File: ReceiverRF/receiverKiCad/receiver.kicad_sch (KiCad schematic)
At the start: 23 parts, among them U1 STM32F103RET6, Y1 Crystal_GND24

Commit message: choix ferrite bead et footprint
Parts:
- FB?: footprint (none) -> Footprints:Ferrite_0603
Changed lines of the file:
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@@
 			)
 		)
-		(property "Footprint" ""
+		(property "Footprint" "Footprints:Ferrite_0603"
 			(at 187.96 35.052 90)
 			(effects
@@
 			)
 		)
-		(property "Datasheet" "Ferrite bead"
+		(property "Datasheet" "https://www.digikey.ca/en/products/detail/vishay-dale/ILBB0603ER121V/2574888"
 			(at 187.96 36.83 0)
 			(effects
@@
 			)
 		)
-		(property "Description" ""
+		(property "Description" "120 ohm @ 100 MHz"
 			(at 187.96 36.83 0)
 			(effects

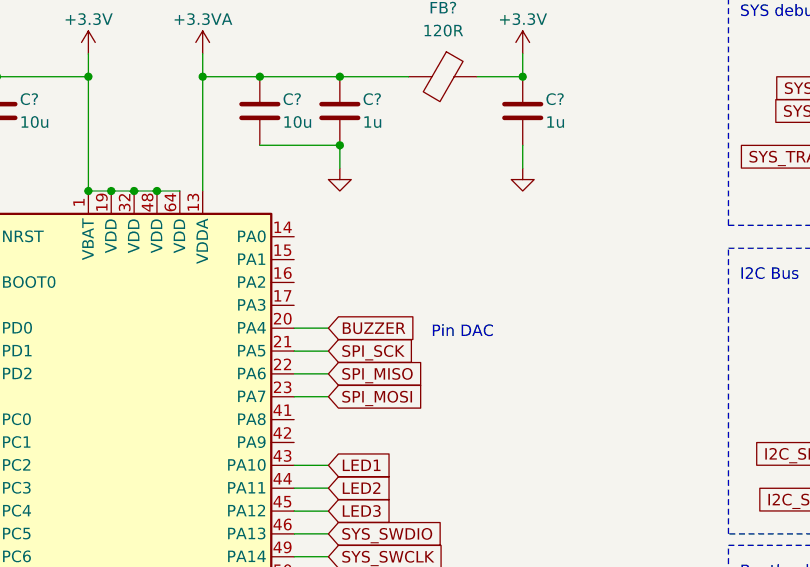
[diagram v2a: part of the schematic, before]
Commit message: Corrige path footprints
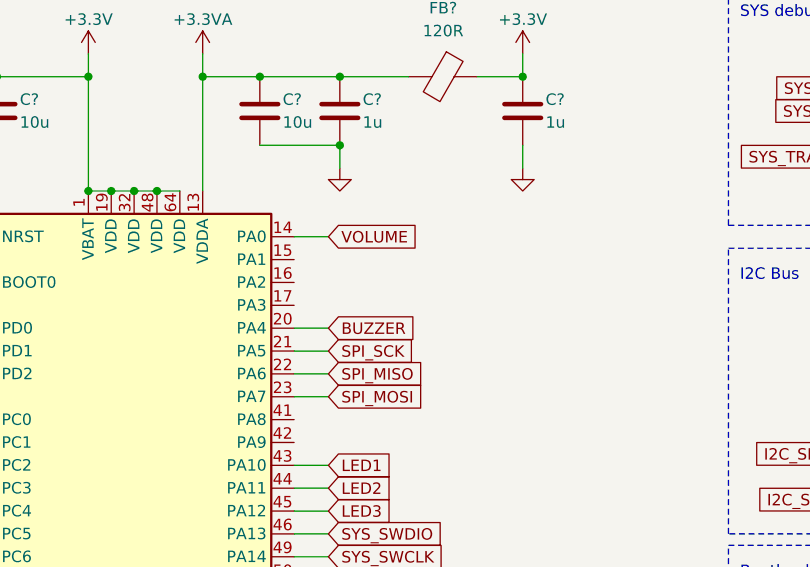
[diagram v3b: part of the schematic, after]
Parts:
- U1: footprint footprint-receiver:LQFP64-10x10mm -> Footprints:LQFP64-10x10mm
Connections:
- net VOLUME: now reaches U1.14 (PA0)
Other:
- note removed: "Pin DAC"
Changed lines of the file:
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@@
+	(wire
+		(pts
+			(xy 171.45 54.61) (xy 175.26 54.61)
+		)
+		(stroke
+			(width 0)
+			(type default)
+		)
+	)
 	(wire
 		(pts
@@
 		)
 	)
-	(text "Pin DAC"
-		(exclude_from_sim no)
-		(at 186.69 66.04 0)
-		(effects
-			(font
-				(size 1.27 1.27)
-			)
-			(justify left bottom)
-		)
-	)
 	(text "SYS debug\n"
 		(exclude_from_sim no)
@@
 		(property "Intersheetrefs" "${INTERSHEET_REFS}"
 			(at 186.8328 135.89 0)
+			(effects
+				(font
+					(size 1.27 1.27)
+				)
+				(justify left)
+				(hide yes)
+			)
+		)
+	)
+	(global_label "VOLUME"
+		(shape input)
+		(at 175.26 54.61 0)
+		(fields_autoplaced yes)
+		(effects
+			(font
+				(size 1.27 1.27)
+			)
+			(justify left)
+		)
+		(property "Intersheetrefs" "${INTERSHEET_REFS}"
+			(at 185.6233 54.61 0)
 			(effects
 				(font
@@
 			)
 		)
-		(property "Footprint" "footprint-receiver:LQFP64-10x10mm"
+		(property "Footprint" "Footprints:LQFP64-10x10mm"
 			(at 138.43 140.97 0)
 			(effects

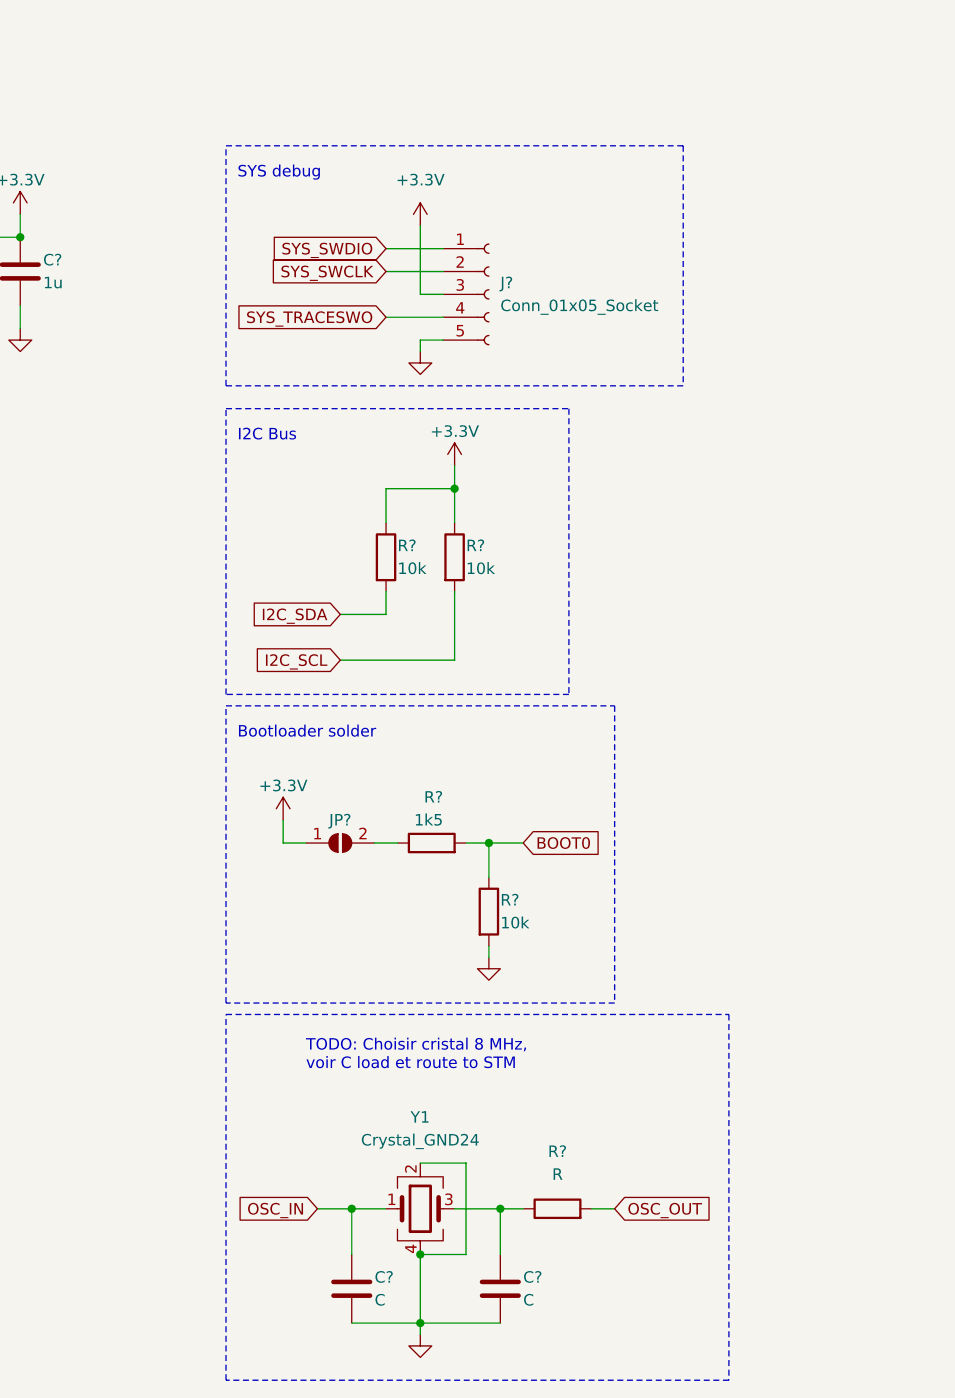
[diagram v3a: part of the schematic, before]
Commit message: Choix cristal 8MHz et Connecteur SMA. Footprint et documentation
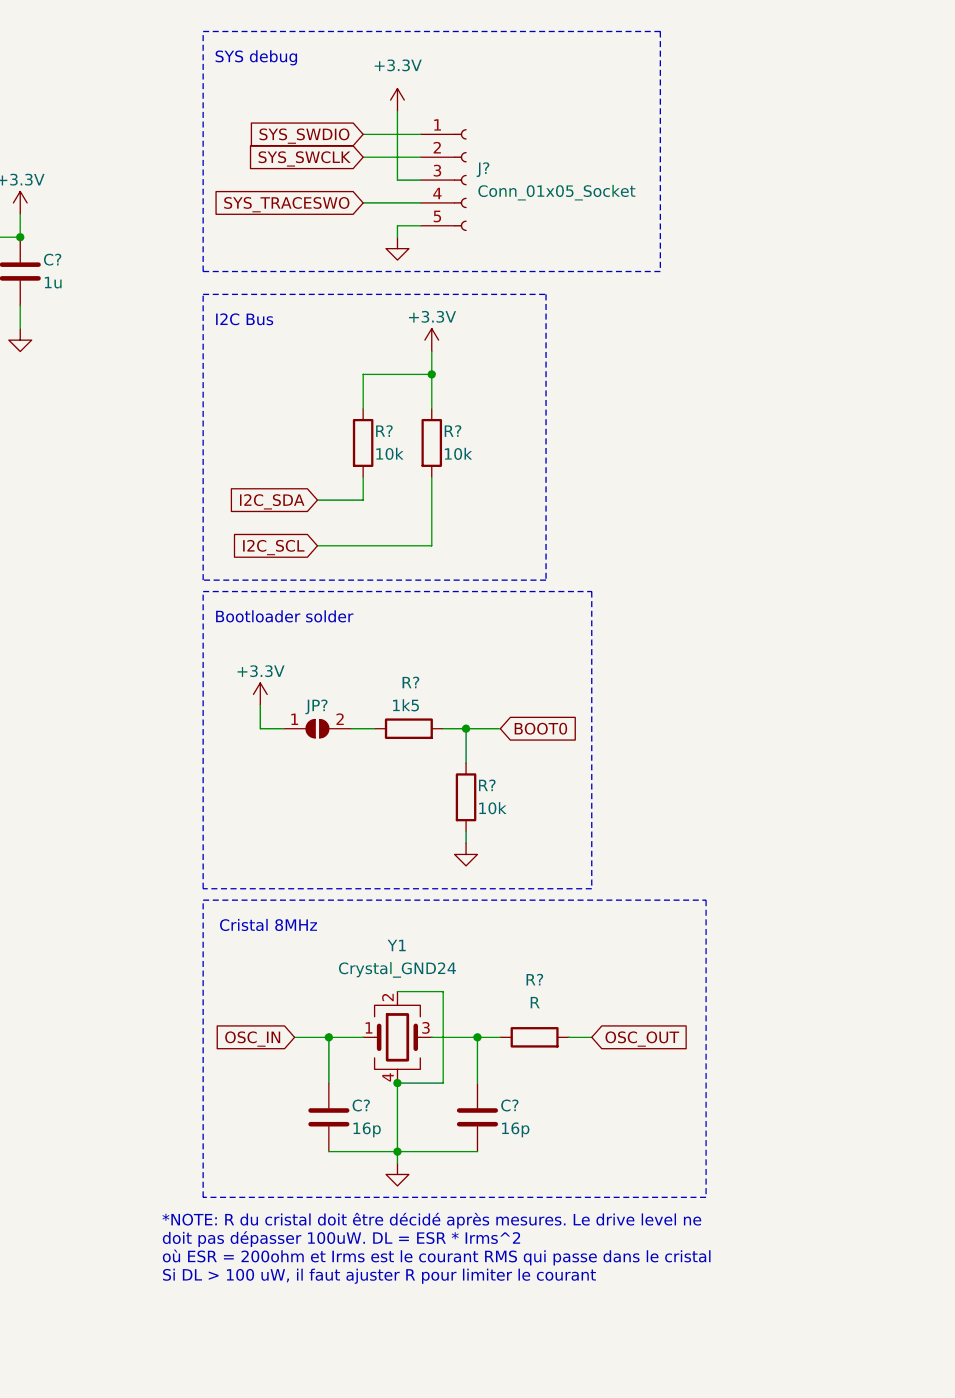
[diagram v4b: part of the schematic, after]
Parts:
- C? (x2): value C -> 16p
- Y1: footprint (none) -> Footprints:Crystal
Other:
- note added: "*NOTE: R du cristal doit être décidé après mesures. Le drive level ne doit pas dépasser 100uW. DL = ESR * Irms^2 où ESR = 200ohm et Irms est le courant RMS qui passe dans le cristal Si DL > 100 uW, il faut ajuster R pour limiter le courant"
- note added: "Cristal 8MHz"
- note removed: "TODO: Choisir cristal 8 MHz, voir C load et route to STM"
- moved on the sheet: C?, J?, JP?, R?, Y1

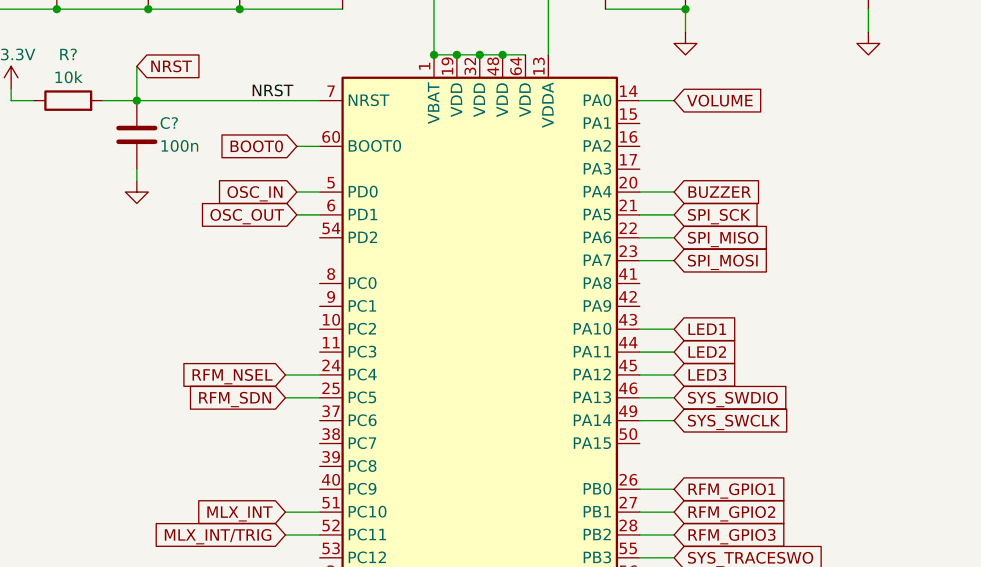
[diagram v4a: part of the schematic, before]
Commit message: Buzzer et diode. Toutes les pièces importantes sont choisies et footprint
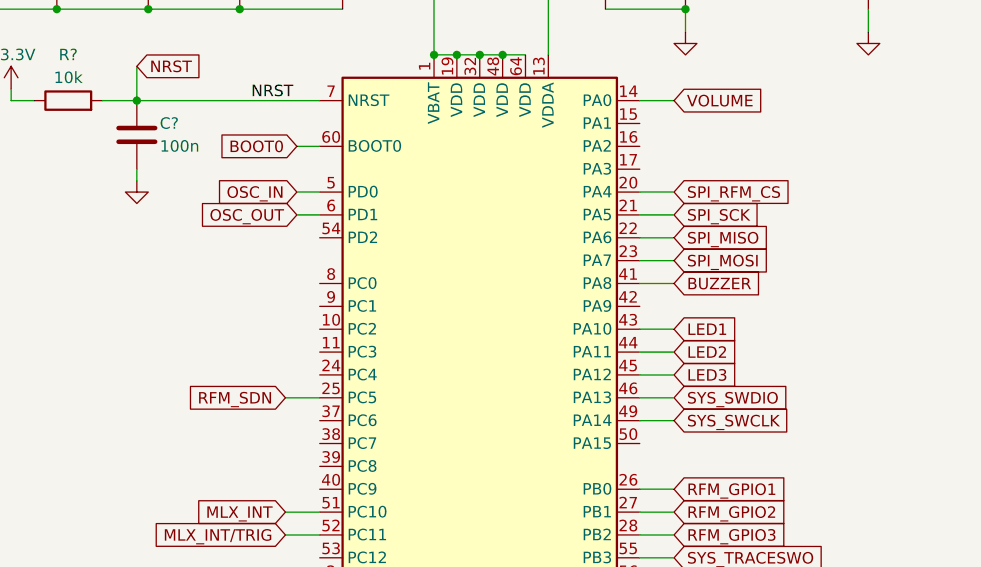
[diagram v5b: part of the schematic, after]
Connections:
- net BUZZER: now also U1.41 (PA8); no longer U1.20 (PA4)
- net RFM_NSEL: no longer names the net of U1.24 (PC4)
- new net SPI_RFM_CS: U1.20 (PA4)

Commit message: Identifiants des symboles
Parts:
- gave numbers to parts that had none: 21
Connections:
- no-connect marks 0 -> 24
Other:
- moved on the sheet: I2C_R1

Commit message: Footprint et choix composantes mineures (résistances et condo)
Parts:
- CSTL_C1, CSTL_C2, STM_C1, STM_C10, STM_C2, STM_C3, STM_C4, STM_C5: footprint (none) -> Capacitor_SMD:C_0402_1005Metric
- I2C_R1, I2C_R2, STM_R1, STM_R3, STM_R4: footprint (none) -> Resistor_SMD:R_0402_1005Metric
- J2: footprint (none) -> Connector_PinHeader_2.00mm:PinHeader_1x05_P2.00mm_Vertical
- JP1: footprint (none) -> Jumper:SolderJumper-2_P1.3mm_Open_TrianglePad1.0x1.5mm
- STM_C6, STM_C7: footprint (none) -> Capacitor_SMD:C_1206_3216Metric
- STM_C8, STM_C9: footprint (none) -> Capacitor_SMD:C_0603_1608Metric
- STM_R2: footprint (none) -> Resistor_SMD:R_1206_3216Metric
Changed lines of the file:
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@@
 			)
 		)
-		(property "Footprint" ""
+		(property "Footprint" "Resistor_SMD:R_1206_3216Metric"
 			(at 240.03 93.218 90)
 			(effects
@@
 			)
 		)
-		(property "Footprint" ""
+		(property "Footprint" "Capacitor_SMD:C_0402_1005Metric"
 			(at 248.6152 138.43 0)
 			(effects
@@
 			)
 		)
-		(property "Footprint" ""
+		(property "Footprint" "Resistor_SMD:R_0402_1005Metric"
 			(at 107.95 56.388 90)
 			(effects
@@
 			)
 		)
-		(property "Footprint" ""
+		(property "Footprint" "Capacitor_SMD:C_1206_3216Metric"
 			(at 139.3952 44.45 0)
 			(effects
@@
 			)
 		)
-		(property "Footprint" ""
+		(property "Footprint" "Jumper:SolderJumper-2_P1.3mm_Open_TrianglePad1.0x1.5mm"
 			(at 229.87 91.44 0)
 			(effects
@@
 			)
 		)
-		(property "Footprint" ""
+		(property "Footprint" "Resistor_SMD:R_0402_1005Metric"
 			(at 230.632 59.69 90)
 			(effects
@@
 			)
 		)
-		(property "Footprint" ""
+		(property "Footprint" "Capacitor_SMD:C_0402_1005Metric"
 			(at 97.4852 44.45 0)
 			(effects
@@
 			)
 		)
-		(property "Footprint" ""
+		(property "Footprint" "Capacitor_SMD:C_0402_1005Metric"
 			(at 107.6452 44.45 0)
 			(effects
@@
 			)
 		)
-		(property "Footprint" ""
+		(property "Footprint" "Resistor_SMD:R_0402_1005Metric"
 			(at 244.602 99.06 90)
 			(effects
@@
 			)
 		)
-		(property "Footprint" ""
+		(property "Footprint" "Capacitor_SMD:C_0402_1005Metric"
 			(at 232.1052 138.43 0)
 			(effects
@@
 			)
 		)
-		(property "Footprint" ""
+		(property "Footprint" "Capacitor_SMD:C_0603_1608Metric"
 			(at 197.8152 44.45 0)
 			(effects
@@
 			)
 		)
-		(property "Footprint" ""
+		(property "Footprint" "Capacitor_SMD:C_0603_1608Metric"
 			(at 177.4952 44.45 0)
 			(effects
@@
 			)
 		)
-		(property "Footprint" ""
+		(property "Footprint" "Capacitor_SMD:C_0402_1005Metric"
 			(at 117.8052 44.45 0)
 			(effects
@@
 			)
 		)
-		(property "Footprint" ""
+		(property "Footprint" "Resistor_SMD:R_0402_1005Metric"
 			(at 254 127.508 90)
 			(effects
@@
 			)
 		)
-		(property "Footprint" ""
+		(property "Footprint" "Capacitor_SMD:C_1206_3216Metric"
 			(at 168.6052 44.45 0)
 			(effects
@@
 			)
 		)
-		(property "Footprint" ""
+		(property "Footprint" "Connector_PinHeader_2.00mm:PinHeader_1x05_P2.00mm_Vertical"
 			(at 246.38 30.48 0)
 			(effects
@@
 			)
 		)
-		(property "Footprint" ""
+		(property "Footprint" "Capacitor_SMD:C_0402_1005Metric"
 			(at 116.5352 62.23 0)
 			(effects
@@
 			)
 		)
-		(property "Footprint" ""
+		(property "Footprint" "Capacitor_SMD:C_0402_1005Metric"
 			(at 87.3252 44.45 0)
 			(effects
@@
 			)
 		)
-		(property "Footprint" ""
+		(property "Footprint" "Capacitor_SMD:C_0402_1005Metric"
 			(at 127.9652 44.45 0)
 			(effects
@@
 			)
 		)
-		(property "Footprint" ""
+		(property "Footprint" "Resistor_SMD:R_0402_1005Metric"
 			(at 240.792 59.69 90)
 			(effects

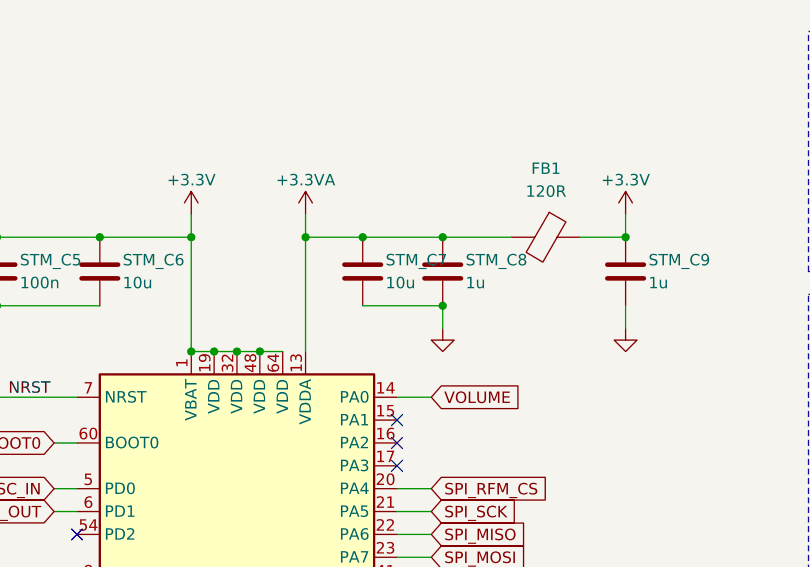
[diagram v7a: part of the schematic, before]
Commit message: Début PCB. Groupement et placement des composantes.
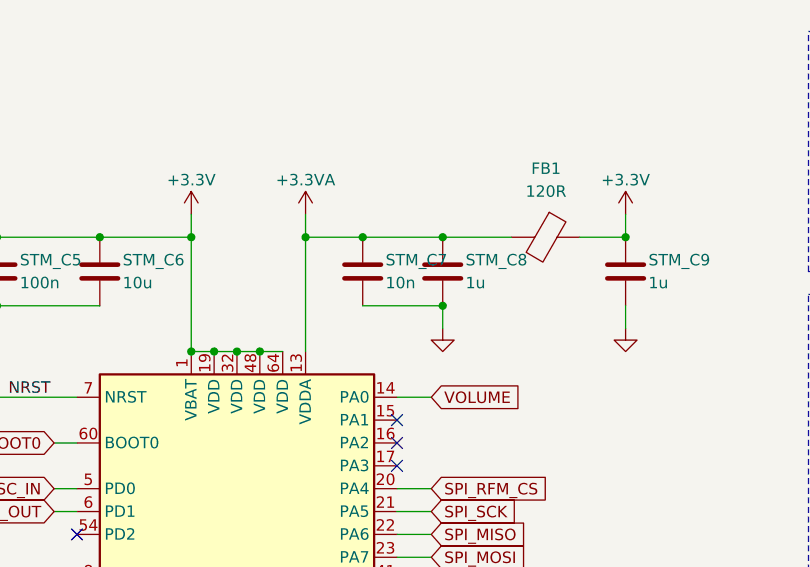
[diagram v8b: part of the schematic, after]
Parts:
- STM_C7: value 10u -> 10n; footprint Capacitor_SMD:C_1206_3216Metric -> Capacitor_SMD:C_0402_1005Metric
- STM_R2: footprint Resistor_SMD:R_1206_3216Metric -> Resistor_SMD:R_0402_1005Metric
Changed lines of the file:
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@@
 			)
 		)
-		(property "Footprint" "Resistor_SMD:R_1206_3216Metric"
+		(property "Footprint" "Resistor_SMD:R_0402_1005Metric"
 			(at 240.03 93.218 90)
 			(effects
@@
 			)
 		)
-		(property "Value" "10u"
+		(property "Value" "10n"
 			(at 170.18 41.91 0)
 			(effects
@@
 			)
 		)
-		(property "Footprint" "Capacitor_SMD:C_1206_3216Metric"
+		(property "Footprint" "Capacitor_SMD:C_0402_1005Metric"
 			(at 168.6052 44.45 0)
 			(effects
